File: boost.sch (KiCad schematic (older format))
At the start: 13 parts, among them SW1 SW_SPST, U2 TPS61022

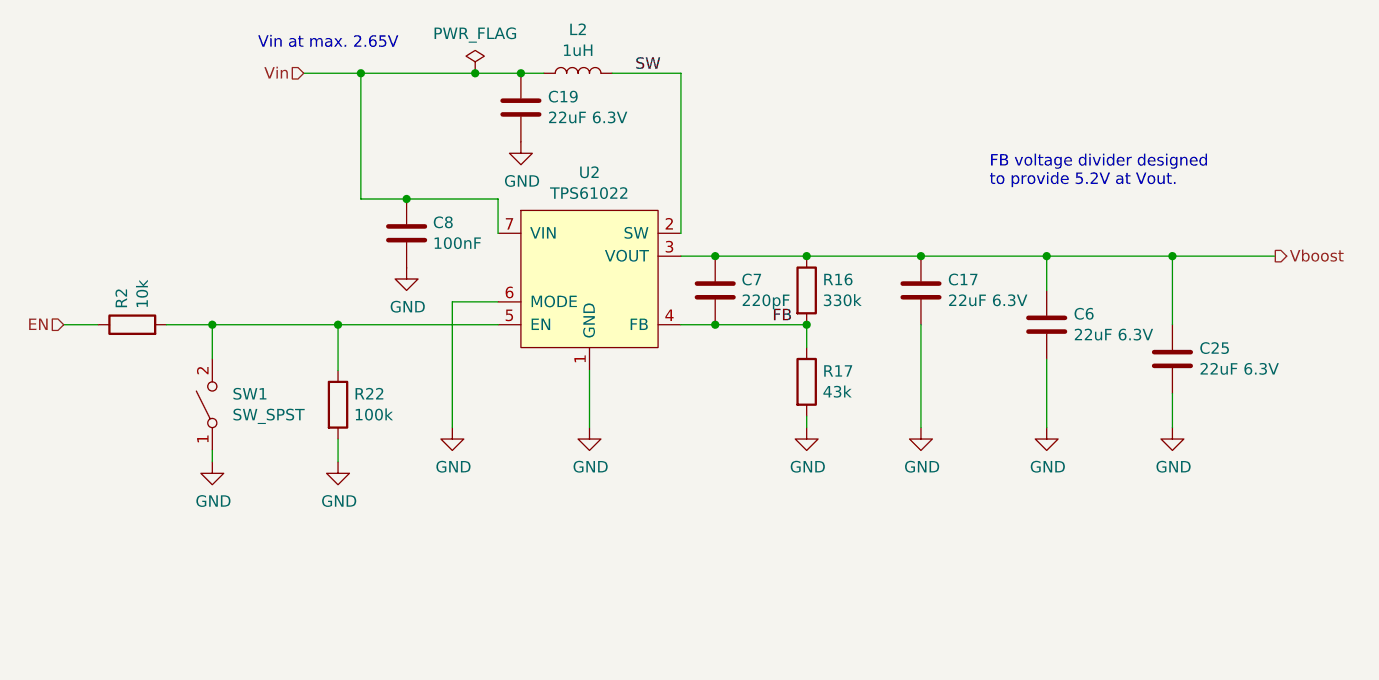
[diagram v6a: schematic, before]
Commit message: Isolated CAN bus implementation
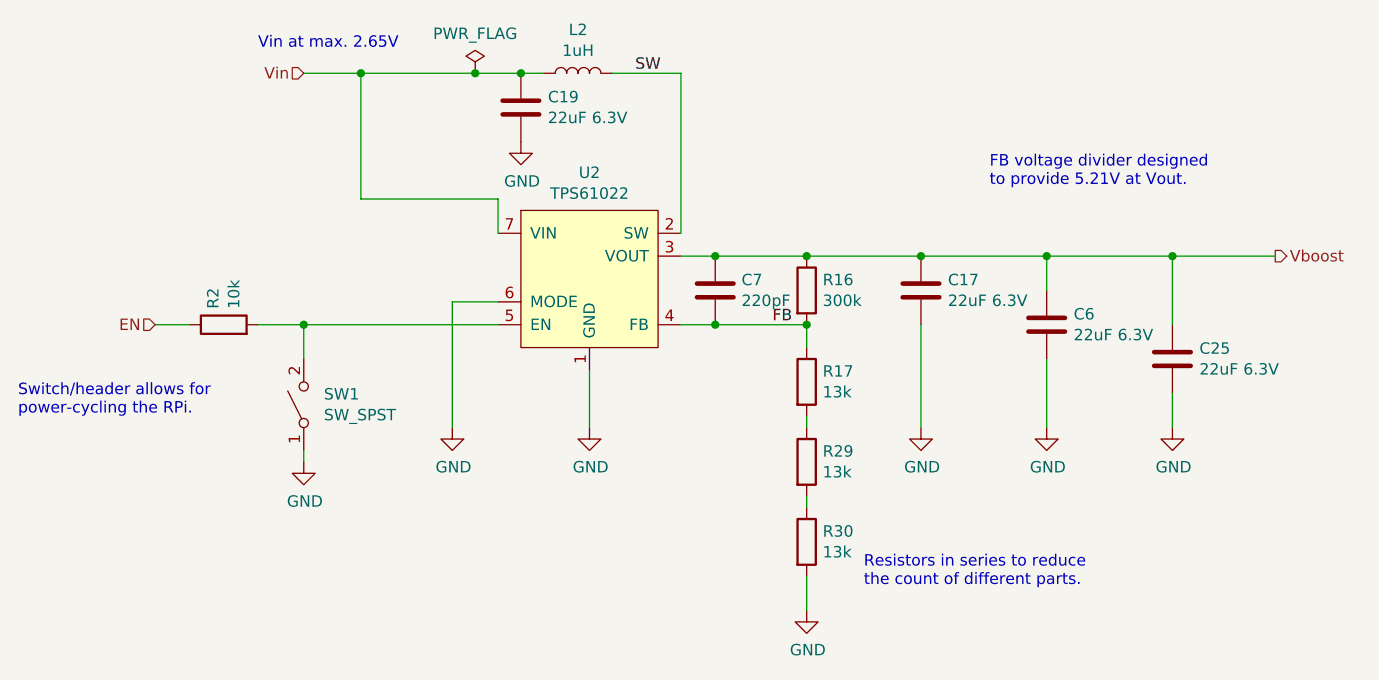
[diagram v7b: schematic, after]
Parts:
- removed C8: 100nF, Capacitor_SMD:C_0603_1608Metric_Pad1.05x0.95mm_HandSolder, symbol Device:C
- removed R22: 100k, Resistor_SMD:R_0603_1608Metric_Pad1.05x0.95mm_HandSolder, symbol Device:R
- added R29, R30: 13k, Resistor_SMD:R_0603_1608Metric, symbol Device:R
- C17, C19, C25, C6: footprint Capacitor_SMD:C_0805_2012Metric_Pad1.15x1.40mm_HandSolder -> Capacitor_SMD:C_0805_2012Metric
- C7: footprint Capacitor_SMD:C_0603_1608Metric_Pad1.05x0.95mm_HandSolder -> Capacitor_SMD:C_0603_1608Metric
- R16: value 330k -> 300k; footprint Resistor_SMD:R_0603_1608Metric_Pad1.05x0.95mm_HandSolder -> Resistor_SMD:R_0603_1608Metric; LCSC C23137 -> (none)
- R17: value 43k -> 13k; footprint Resistor_SMD:R_0603_1608Metric_Pad1.05x0.95mm_HandSolder -> Resistor_SMD:R_0603_1608Metric; LCSC C23172 -> (none)
- R2: footprint Resistor_SMD:R_0603_1608Metric_Pad1.05x0.95mm_HandSolder -> Resistor_SMD:R_0603_1608Metric
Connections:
- net GND: now also R30.2; no longer R17.2
- new net: R17.2, R29.1
- new net: R29.2, R30.1
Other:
- note added: "FB voltage divider designed\nto provide 5.21V at Vout."
- note added: "Resistors in series to reduce\nthe count of different parts."
- note added: "Switch/header allows for\npower-cycling the RPi."
- note removed: "FB voltage divider designed\nto provide 5.2V at Vout."
- moved on the sheet: R2, SW1
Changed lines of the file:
@@
 F 0 "C17" H 4968 2496 50  0000 L CNN
 F 1 "22uF 6.3V" H 4968 2405 50  0000 L CNN
-F 2 "Capacitor_SMD:C_0805_2012Metric_Pad1.15x1.40mm_HandSolder" H 4888 2300 50  0001 C CNN
+F 2 "Capacitor_SMD:C_0805_2012Metric" H 4888 2300 50  0001 C CNN
 F 3 "~" H 4850 2450 50  0001 C CNN
 F 4 "C45783" H 4850 2450 50  0001 C CNN "LCSC"
@@
 $EndComp
 Wire Wire Line
-	3000 2050 2600 2050
-Wire Wire Line
 	2400 1500 2900 1500
 Wire Wire Line
@@
 AR Path="/5CA73F16/5CA6B51B" Ref="R16"  Part="1"
 F 0 "R16" H 4420 2496 50  0000 L CNN
-F 1 "330k" H 4420 2405 50  0000 L CNN
-F 2 "Resistor_SMD:R_0603_1608Metric_Pad1.05x0.95mm_HandSolder" V 4280 2450 50  0001 C CNN
+F 1 "300k" H 4420 2405 50  0000 L CNN
+F 2 "Resistor_SMD:R_0603_1608Metric" V 4280 2450 50  0001 C CNN
 F 3 "~" H 4350 2450 50  0001 C CNN
-F 4 "C23137" H 4350 2450 50  0001 C CNN "LCSC"
+F 4 "" H 4350 2450 50  0001 C CNN "LCSC"
 	1    4350 2450
 	1    0    0    -1
@@
 AR Path="/5CA73F16/5CA6B522" Ref="R17"  Part="1"
 F 0 "R17" H 4420 2896 50  0000 L CNN
-F 1 "43k" H 4420 2805 50  0000 L CNN
-F 2 "Resistor_SMD:R_0603_1608Metric_Pad1.05x0.95mm_HandSolder" V 4280 2850 50  0001 C CNN
+F 1 "13k" H 4420 2805 50  0000 L CNN
+F 2 "Resistor_SMD:R_0603_1608Metric" V 4280 2850 50  0001 C CNN
 F 3 "~" H 4350 2850 50  0001 C CNN
-F 4 "C23172" H 4350 2850 50  0001 C CNN "LCSC"
+F 4 "" H 4350 2850 50  0001 C CNN "LCSC"
 	1    4350 2850
 	1    0    0    -1
@@
 L power:GND #PWR?
 U 1 1 5CA6B529
-P 4350 3050
+P 4350 3850
 AR Path="/5CA6B529" Ref="#PWR?"  Part="1"
 AR Path="/5C3480BB/5CA6B529" Ref="#PWR?"  Part="1"
 AR Path="/5CA73F16/5CA6B529" Ref="#PWR045"  Part="1"
-F 0 "#PWR045" H 4350 2800 50  0001 C CNN
-F 1 "GND" H 4355 2877 50  0000 C CNN
-F 2 "" H 4350 3050 50  0001 C CNN
-F 3 "" H 4350 3050 50  0001 C CNN
-	1    4350 3050
+F 0 "#PWR045" H 4350 3600 50  0001 C CNN
+F 1 "GND" H 4355 3677 50  0000 C CNN
+F 2 "" H 4350 3850 50  0001 C CNN
+F 3 "" H 4350 3850 50  0001 C CNN
+	1    4350 3850
 	1    0    0    -1
 $EndComp
@@
 Connection ~ 4350 2600
 Wire Wire Line
-	4350 3050 4350 3000
+	4350 3850 4350 3700
 Wire Wire Line
 	2150 1500 2400 1500
@@
 	3800 2600 3950 2600
 Text Notes 5150 2000 0    50   ~ 0
-FB voltage divider designed\nto provide 5.2V at Vout.
+FB voltage divider designed\nto provide 5.21V at Vout.
 Text HLabel 6400 2300 2    50   Output ~ 0
 Vboost
@@
 F 0 "C19" H 3218 1696 50  0000 L CNN
 F 1 "22uF 6.3V" H 3218 1605 50  0000 L CNN
-F 2 "Capacitor_SMD:C_0805_2012Metric_Pad1.15x1.40mm_HandSolder" H 3138 1500 50  0001 C CNN
+F 2 "Capacitor_SMD:C_0805_2012Metric" H 3138 1500 50  0001 C CNN
 F 3 "~" H 3100 1650 50  0001 C CNN
 F 4 "C45783" H 3100 1650 50  0001 C CNN "LCSC"
@@
 	1    0    0    -1
 $EndComp
-Text HLabel 1100 2600 0    50   Input ~ 0
+Text HLabel 1500 2600 0    50   Input ~ 0
 EN
 $Comp
@@
 $EndComp
 Wire Wire Line
-	1100 2600 1250 2600
+	1500 2600 1650 2600
 $Comp
 L power:GND #PWR?
@@
 L Switch:SW_SPST SW1
 U 1 1 5D5B325B
-P 1750 2950
-F 0 "SW1" V 1796 2862 50  0000 R CNN
-F 1 "SW_SPST" V 1705 2862 50  0000 R CNN
-F 2 "Connector_PinHeader_2.54mm:PinHeader_1x02_P2.54mm_Vertical" H 1750 2950 50  0001 C CNN
-F 3 "~" H 1750 2950 50  0001 C CNN
-	1    1750 2950
+P 2150 2950
+F 0 "SW1" V 2196 2862 50  0000 R CNN
+F 1 "SW_SPST" V 2105 2862 50  0000 R CNN
+F 2 "Connector_PinHeader_2.54mm:PinHeader_1x02_P2.54mm_Vertical" H 2150 2950 50  0001 C CNN
+F 3 "~" H 2150 2950 50  0001 C CNN
+	1    2150 2950
 	0    -1   -1   0
 $EndComp
@@
 L Device:R R?
 U 1 1 5D5B16A2
-P 1400 2600
+P 1800 2600
 AR Path="/5D5B16A2" Ref="R?"  Part="1"
 AR Path="/5C3480BB/5D5B16A2" Ref="R?"  Part="1"
 AR Path="/5CA73F16/5D5B16A2" Ref="R2"  Part="1"
-F 0 "R2" H 1470 2646 50  0000 L CNN
-F 1 "10k" H 1470 2555 50  0000 L CNN
-F 2 "Resistor_SMD:R_0603_1608Metric_Pad1.05x0.95mm_HandSolder" V 1330 2600 50  0001 C CNN
-F 3 "~" H 1400 2600 50  0001 C CNN
-F 4 "C25804" H 1400 2600 50  0001 C CNN "LCSC"
-	1    1400 2600
+F 0 "R2" H 1870 2646 50  0000 L CNN
+F 1 "10k" H 1870 2555 50  0000 L CNN
+F 2 "Resistor_SMD:R_0603_1608Metric" V 1730 2600 50  0001 C CNN
+F 3 "~" H 1800 2600 50  0001 C CNN
+F 4 "C25804" H 1800 2600 50  0001 C CNN "LCSC"
+	1    1800 2600
 	0    -1   -1   0
 $EndComp
 Wire Wire Line
-	1550 2600 1750 2600
-Wire Wire Line
-	1750 2750 1750 2600
-Connection ~ 1750 2600
+	1950 2600 2150 2600
+Wire Wire Line
+	2150 2750 2150 2600
+Connection ~ 2150 2600
 $Comp
 L power:GND #PWR?
 U 1 1 5D5B5E50
-P 1750 3200
+P 2150 3200
 AR Path="/5D5B5E50" Ref="#PWR?"  Part="1"
 AR Path="/5C3480BB/5D5B5E50" Ref="#PWR?"  Part="1"
 AR Path="/5CA73F16/5D5B5E50" Ref="#PWR0108"  Part="1"
-F 0 "#PWR0108" H 1750 2950 50  0001 C CNN
-F 1 "GND" H 1755 3027 50  0000 C CNN
-F 2 "" H 1750 3200 50  0001 C CNN
-F 3 "" H 1750 3200 50  0001 C CNN
-	1    1750 3200
-	1    0    0    -1
-$EndComp
-Wire Wire Line
-	1750 3200 1750 3150
+F 0 "#PWR0108" H 2150 2950 50  0001 C CNN
+F 1 "GND" H 2155 3027 50  0000 C CNN
+F 2 "" H 2150 3200 50  0001 C CNN
+F 3 "" H 2150 3200 50  0001 C CNN
+	1    2150 3200
+	1    0    0    -1
+$EndComp
+Wire Wire Line
+	2150 3200 2150 3150
 $Comp
 L Device:C C?
@@
 F 0 "C6" H 5518 2646 50  0000 L CNN
 F 1 "22uF 6.3V" H 5518 2555 50  0000 L CNN
-F 2 "Capacitor_SMD:C_0805_2012Metric_Pad1.15x1.40mm_HandSolder" H 5438 2450 50  0001 C CNN
+F 2 "Capacitor_SMD:C_0805_2012Metric" H 5438 2450 50  0001 C CNN
 F 3 "~" H 5400 2600 50  0001 C CNN
 F 4 "C45783" H 5400 2600 50  0001 C CNN "LCSC"
@@
 F 0 "C7" H 4065 2496 50  0000 L CNN
 F 1 "220pF" H 4065 2405 50  0000 L CNN
-F 2 "Capacitor_SMD:C_0603_1608Metric_Pad1.05x0.95mm_HandSolder" H 3988 2300 50  0001 C CNN
+F 2 "Capacitor_SMD:C_0603_1608Metric" H 3988 2300 50  0001 C CNN
 F 3 "~" H 3950 2450 50  0001 C CNN
 F 4 "C1603" H 3950 2450 50  0001 C CNN "LCSC"
@@
 $EndComp
 Wire Wire Line
-	1750 2600 2300 2600
-$Comp
-L Device:R R?
-U 1 1 5D91DD8E
-P 2300 2950
-AR Path="/5D91DD8E" Ref="R?"  Part="1"
-AR Path="/5C3480BB/5D91DD8E" Ref="R?"  Part="1"
-AR Path="/5CA73F16/5D91DD8E" Ref="R22"  Part="1"
-F 0 "R22" H 2370 2996 50  0000 L CNN
-F 1 "100k" H 2370 2905 50  0000 L CNN
-F 2 "Resistor_SMD:R_0603_1608Metric_Pad1.05x0.95mm_HandSolder" V 2230 2950 50  0001 C CNN
-F 3 "~" H 2300 2950 50  0001 C CNN
-F 4 "C25803" H 2300 2950 50  0001 C CNN "LCSC"
-	1    2300 2950
-	1    0    0    -1
-$EndComp
-Wire Wire Line
-	2300 2800 2300 2600
-Connection ~ 2300 2600
-Wire Wire Line
-	2300 2600 3000 2600
-Wire Wire Line
-	2300 3100 2300 3200
-$Comp
-L power:GND #PWR?
-U 1 1 5D91E379
-P 2300 3200
-AR Path="/5D91E379" Ref="#PWR?"  Part="1"
-AR Path="/5C3480BB/5D91E379" Ref="#PWR?"  Part="1"
-AR Path="/5CA73F16/5D91E379" Ref="#PWR025"  Part="1"
-F 0 "#PWR025" H 2300 2950 50  0001 C CNN
-F 1 "GND" H 2305 3027 50  0000 C CNN
-F 2 "" H 2300 3200 50  0001 C CNN
-F 3 "" H 2300 3200 50  0001 C CNN
-	1    2300 3200
-	1    0    0    -1
-$EndComp
-Wire Wire Line
 	3800 1500 3800 2200
 Connection ~ 3100 1500
@@
 	2400 1500 2400 2050
 Connection ~ 2400 1500
-$Comp
-L Device:C C8
-U 1 1 5D9259A2
-P 2600 2200
-F 0 "C8" H 2715 2246 50  0000 L CNN
-F 1 "100nF" H 2715 2155 50  0000 L CNN
-F 2 "Capacitor_SMD:C_0603_1608Metric_Pad1.05x0.95mm_HandSolder" H 2638 2050 50  0001 C CNN
-F 3 "~" H 2600 2200 50  0001 C CNN
-F 4 "C14663" H 2600 2200 50  0001 C CNN "LCSC"
-	1    2600 2200
-	1    0    0    -1
-$EndComp
 Wire Wire Line
 	3000 2050 3000 2200
-Connection ~ 2600 2050
-Wire Wire Line
-	2600 2050 2400 2050
-$Comp
-L power:GND #PWR?
-U 1 1 5D9260DB
-P 2600 2350
-AR Path="/5D9260DB" Ref="#PWR?"  Part="1"
-AR Path="/5C3480BB/5D9260DB" Ref="#PWR?"  Part="1"
-AR Path="/5CA73F16/5D9260DB" Ref="#PWR049"  Part="1"
-F 0 "#PWR049" H 2600 2100 50  0001 C CNN
-F 1 "GND" H 2605 2177 50  0000 C CNN
-F 2 "" H 2600 2350 50  0001 C CNN
-F 3 "" H 2600 2350 50  0001 C CNN
-	1    2600 2350
-	1    0    0    -1
-$EndComp
 $Comp
 L power:PWR_FLAG #FLG0101
@@
 F 0 "C25" H 6068 2796 50  0000 L CNN
 F 1 "22uF 6.3V" H 6068 2705 50  0000 L CNN
-F 2 "Capacitor_SMD:C_0805_2012Metric_Pad1.15x1.40mm_HandSolder" H 5988 2600 50  0001 C CNN
+F 2 "Capacitor_SMD:C_0805_2012Metric" H 5988 2600 50  0001 C CNN
 F 3 "~" H 5950 2750 50  0001 C CNN
 F 4 "C45783" H 5950 2750 50  0001 C CNN "LCSC"
@@
 Wire Wire Line
 	4850 3050 4850 2600
+$Comp
+L Device:R R?
+U 1 1 5F48CB1D
+P 4350 3200
+AR Path="/5F48CB1D" Ref="R?"  Part="1"
+AR Path="/5C3480BB/5F48CB1D" Ref="R?"  Part="1"
+AR Path="/5CA73F16/5F48CB1D" Ref="R29"  Part="1"
+F 0 "R29" H 4420 3246 50  0000 L CNN
+F 1 "13k" H 4420 3155 50  0000 L CNN
+F 2 "Resistor_SMD:R_0603_1608Metric" V 4280 3200 50  0001 C CNN
+F 3 "~" H 4350 3200 50  0001 C CNN
+F 4 "" H 4350 3200 50  0001 C CNN "LCSC"
+	1    4350 3200
+	1    0    0    -1
+$EndComp
+Wire Wire Line
+	4350 3050 4350 3000
+$Comp
+L Device:R R?
+U 1 1 5F48D0EA
+P 4350 3550
+AR Path="/5F48D0EA" Ref="R?"  Part="1"
+AR Path="/5C3480BB/5F48D0EA" Ref="R?"  Part="1"
+AR Path="/5CA73F16/5F48D0EA" Ref="R30"  Part="1"
+F 0 "R30" H 4420 3596 50  0000 L CNN
+F 1 "13k" H 4420 3505 50  0000 L CNN
+F 2 "Resistor_SMD:R_0603_1608Metric" V 4280 3550 50  0001 C CNN
+F 3 "~" H 4350 3550 50  0001 C CNN
+F 4 "" H 4350 3550 50  0001 C CNN "LCSC"
+	1    4350 3550
+	1    0    0    -1
+$EndComp
+Wire Wire Line
+	4350 3400 4350 3350
+Text Notes 900  3000 0    50   ~ 0
+Switch/header allows for\npower-cycling the RPi.
+Text Notes 4600 3750 0    50   ~ 0
+Resistors in series to reduce\nthe count of different parts.
+Wire Wire Line
+	2150 2600 3000 2600
+Wire Wire Line
+	2400 2050 3000 2050
 $EndSCHEMATC

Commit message: Parts updated to match JLCPCB availability
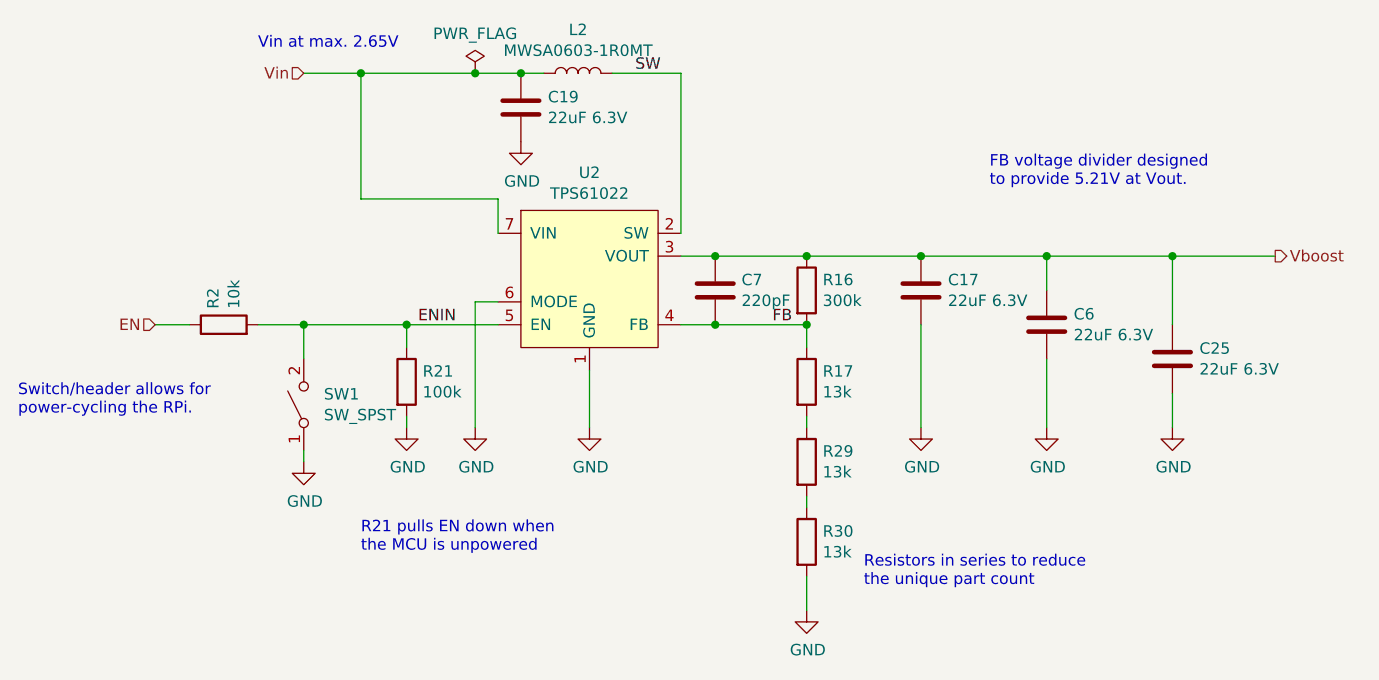
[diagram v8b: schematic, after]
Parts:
- added R21: 100k, Resistor_SMD:R_0603_1608Metric, symbol Device:R
- L2: value 1uH -> MWSA0603-1R0MT
- R16: LCSC (none) -> C23024
- R17, R29, R30: LCSC (none) -> C22797
- U2: Mouser (none) -> 595-TPS61022RWUR
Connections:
- net GND: now also R21.2
- net ENIN: now reaches R2.2, SW1.2 (B), U2.5 (EN)
- net ENIN: now also R21.1
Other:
- note added: "R21 pulls EN down when\nthe MCU is unpowered"
- note added: "Resistors in series to reduce\nthe unique part count"
- note removed: "Resistors in series to reduce\nthe count of different parts."
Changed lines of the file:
@@
 AR Path="/5CA73F16/5CA6B4FC" Ref="L2"  Part="1"
 F 0 "L2" V 3540 1500 50  0000 C CNN
-F 1 "1uH" V 3449 1500 50  0000 C CNN
+F 1 "MWSA0603-1R0MT" V 3449 1500 50  0000 C CNN
 F 2 "Inductor_SMD:L_Abracon_ASPI-0630LR" H 3350 1500 50  0001 C CNN
 F 3 "" H 3350 1500 50  0001 C CNN
@@
 F 2 "Resistor_SMD:R_0603_1608Metric" V 4280 2450 50  0001 C CNN
 F 3 "~" H 4350 2450 50  0001 C CNN
-F 4 "" H 4350 2450 50  0001 C CNN "LCSC"
+F 4 "C23024" H 4350 2450 50  0001 C CNN "LCSC"
 	1    4350 2450
 	1    0    0    -1
@@
 F 2 "Resistor_SMD:R_0603_1608Metric" V 4280 2850 50  0001 C CNN
 F 3 "~" H 4350 2850 50  0001 C CNN
-F 4 "" H 4350 2850 50  0001 C CNN "LCSC"
+F 4 "C22797" H 4350 2850 50  0001 C CNN "LCSC"
 	1    4350 2850
 	1    0    0    -1
@@
 L power:GND #PWR?
 U 1 1 5D5460DA
-P 2800 3050
+P 2900 3050
 AR Path="/5D5460DA" Ref="#PWR?"  Part="1"
 AR Path="/5C3480BB/5D5460DA" Ref="#PWR?"  Part="1"
 AR Path="/5CA73F16/5D5460DA" Ref="#PWR0107"  Part="1"
-F 0 "#PWR0107" H 2800 2800 50  0001 C CNN
-F 1 "GND" H 2805 2877 50  0000 C CNN
-F 2 "" H 2800 3050 50  0001 C CNN
-F 3 "" H 2800 3050 50  0001 C CNN
-	1    2800 3050
+F 0 "#PWR0107" H 2900 2800 50  0001 C CNN
+F 1 "GND" H 2905 2877 50  0000 C CNN
+F 2 "" H 2900 3050 50  0001 C CNN
+F 3 "" H 2900 3050 50  0001 C CNN
+	1    2900 3050
 	1    0    0    -1
 $EndComp
@@
 F 2 "custom:TPS61022RWUR" H 3450 2600 50  0001 C CNN
 F 3 "" H 3450 2600 50  0001 C CNN
+F 4 "595-TPS61022RWUR" H 3400 2400 50  0001 C CNN "Mouser"
 	1    3400 2400
 	1    0    0    -1
@@
 	4850 2300 4350 2300
 Wire Wire Line
-	2800 2500 3000 2500
+	2900 2500 3000 2500
 $Comp
 L Switch:SW_SPST SW1
@@
 $EndComp
 Wire Wire Line
-	2800 3050 2800 2500
+	2900 3050 2900 2500
 Text Notes 1950 1400 0    50   ~ 0
 Vin at max. 2.65V
@@
 F 2 "Resistor_SMD:R_0603_1608Metric" V 4280 3200 50  0001 C CNN
 F 3 "~" H 4350 3200 50  0001 C CNN
-F 4 "" H 4350 3200 50  0001 C CNN "LCSC"
+F 4 "C22797" H 4350 3200 50  0001 C CNN "LCSC"
 	1    4350 3200
 	1    0    0    -1
@@
 F 2 "Resistor_SMD:R_0603_1608Metric" V 4280 3550 50  0001 C CNN
 F 3 "~" H 4350 3550 50  0001 C CNN
-F 4 "" H 4350 3550 50  0001 C CNN "LCSC"
+F 4 "C22797" H 4350 3550 50  0001 C CNN "LCSC"
 	1    4350 3550
 	1    0    0    -1
@@
 Switch/header allows for\npower-cycling the RPi.
 Text Notes 4600 3750 0    50   ~ 0
-Resistors in series to reduce\nthe count of different parts.
-Wire Wire Line
-	2150 2600 3000 2600
+Resistors in series to reduce\nthe unique part count
+Wire Wire Line
+	2150 2600 2600 2600
 Wire Wire Line
 	2400 2050 3000 2050
+Text Label 2650 2600 0    50   ~ 0
+ENIN
+$Comp
+L Device:R R?
+U 1 1 5F480D4D
+P 2600 2850
+AR Path="/5F480D4D" Ref="R?"  Part="1"
+AR Path="/5C3480BB/5F480D4D" Ref="R?"  Part="1"
+AR Path="/5CA73F16/5F480D4D" Ref="R21"  Part="1"
+F 0 "R21" H 2670 2896 50  0000 L CNN
+F 1 "100k" H 2670 2805 50  0000 L CNN
+F 2 "Resistor_SMD:R_0603_1608Metric" V 2530 2850 50  0001 C CNN
+F 3 "~" H 2600 2850 50  0001 C CNN
+F 4 "C25803" H 2600 2850 50  0001 C CNN "LCSC"
+	1    2600 2850
+	1    0    0    -1
+$EndComp
+Connection ~ 2600 2600
+Wire Wire Line
+	2600 2600 3000 2600
+$Comp
+L power:GND #PWR?
+U 1 1 5F481463
+P 2600 3050
+AR Path="/5F481463" Ref="#PWR?"  Part="1"
+AR Path="/5C3480BB/5F481463" Ref="#PWR?"  Part="1"
+AR Path="/5CA73F16/5F481463" Ref="#PWR07"  Part="1"
+F 0 "#PWR07" H 2600 2800 50  0001 C CNN
+F 1 "GND" H 2605 2877 50  0000 C CNN
+F 2 "" H 2600 3050 50  0001 C CNN
+F 3 "" H 2600 3050 50  0001 C CNN
+	1    2600 3050
+	1    0    0    -1
+$EndComp
+Wire Wire Line
+	2600 2700 2600 2600
+Wire Wire Line
+	2600 3000 2600 3050
+Text Notes 2400 3600 0    50   ~ 0
+R21 pulls EN down when\nthe MCU is unpowered
 $EndSCHEMATC
